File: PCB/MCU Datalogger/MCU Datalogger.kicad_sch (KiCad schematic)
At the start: 25 parts, among them U1 24LC1025, U2 24LC1025, U3 DS1337S+, U4 ATMEGA328P-AU, Y1 16 MHz, Y2 32.768 Khz

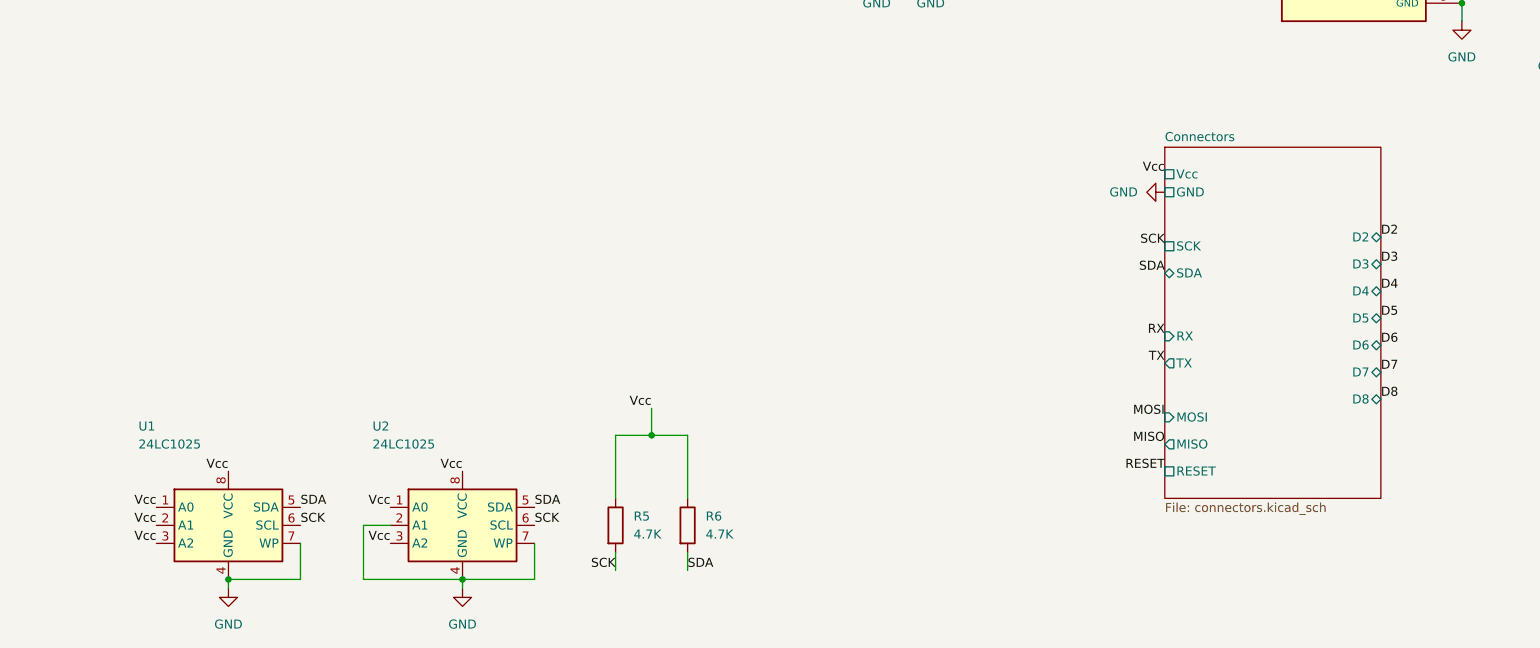
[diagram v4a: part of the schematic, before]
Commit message: Power net class added to Vcc and GND
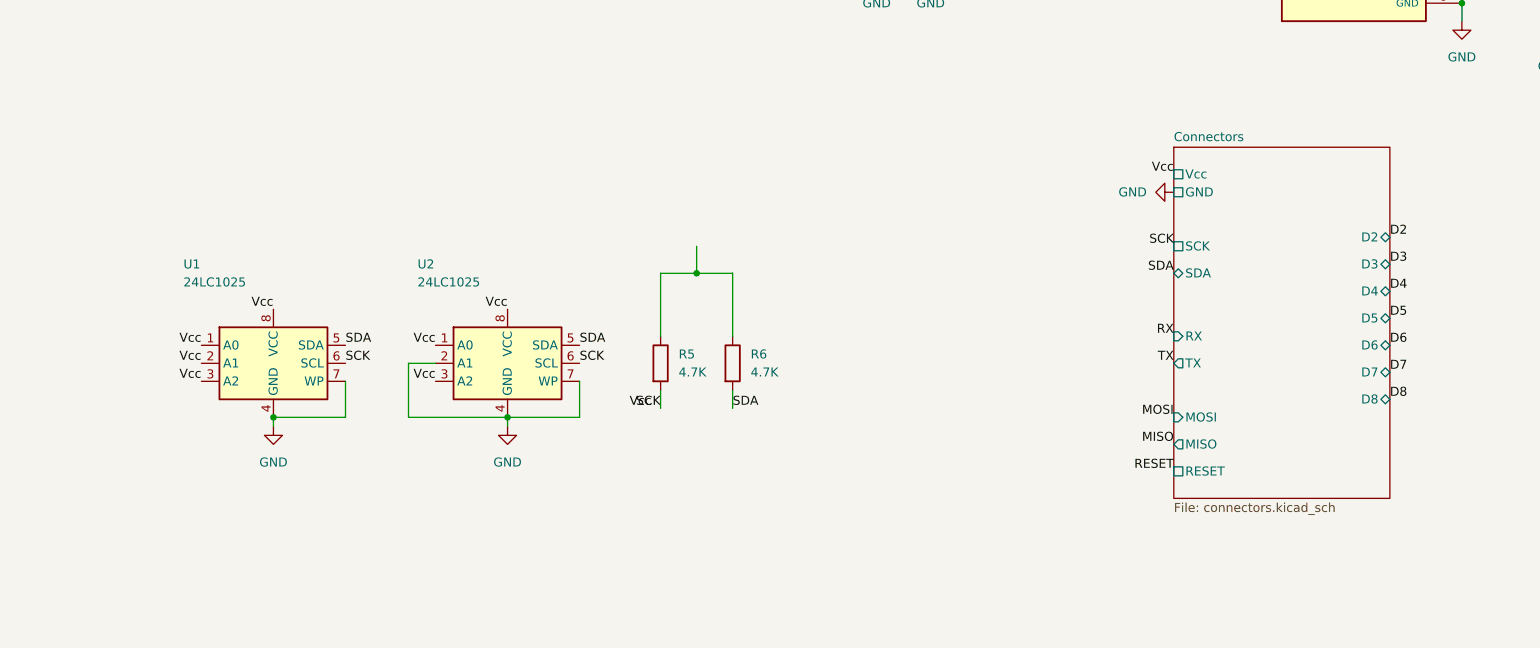
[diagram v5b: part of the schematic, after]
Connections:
- net Vcc: no longer R5.1, R6.1
- new net: R5.1, R6.1
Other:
- moved on the sheet: R5, R6, U1, U2
